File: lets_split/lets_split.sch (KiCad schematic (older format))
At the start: 56 parts, among them P1 USB-rewire, P2 USB_OTG, P3 WS2812-Strip, P4 TRRS jack, SW1 SW_PUSH, SW10 SW_PUSH, SW11 SW_PUSH, SW12 SW_PUSH, SW13 SW_PUSH, SW14 SW_PUSH, SW15 SW_PUSH, SW16 SW_PUSH, SW17 SW_PUSH, SW18 SW_PUSH, SW19 SW_PUSH, SW2 SW_PUSH, SW20 SW_PUSH, SW21 SW_PUSH, SW22 SW_PUSH, SW23 SW_PUSH, SW24 SW_PUSH, SW3 SW_PUSH, SW4 SW_PUSH, SW5 SW_PUSH, SW6 SW_PUSH, SW7 SW_PUSH, SW8 SW_PUSH, SW9 SW_PUSH, U1 ArduinoProMicro

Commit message: Added images of reversible version
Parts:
- P2: symbol USB_OTG -> USB_OTG-RESCUE-lets_split
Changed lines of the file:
@@
-EESchema Schematic File Version 3
+EESchema Schematic File Version 2
+LIBS:lets_split-rescue
 LIBS:power
 LIBS:device
+LIBS:transistors
+LIBS:conn
 LIBS:linear
 LIBS:regul
+LIBS:74xx
+LIBS:cmos4000
 LIBS:adc-dac
 LIBS:memory
@@
 LIBS:digital-audio
 LIBS:philips
+LIBS:display
 LIBS:cypress
 LIBS:siliconi
@@
 LIBS:atmel
 LIBS:contrib
+LIBS:valves
 LIBS:8Bit-MCU
 LIBS:lets_split-cache
@@
 Connection ~ 2275 4550
 $Comp
-L USB_OTG P2
+L USB_OTG-RESCUE-lets_split P2
 U 1 1 59DD5ACB
 P 1825 4125

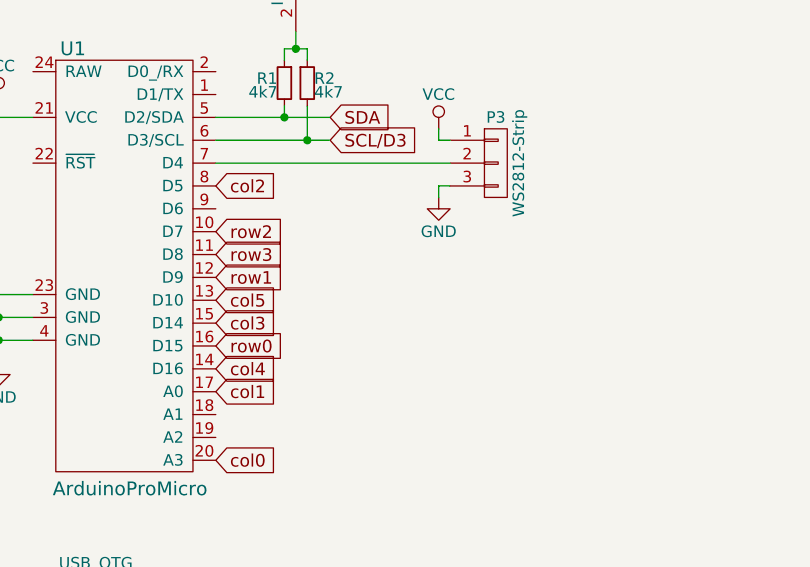
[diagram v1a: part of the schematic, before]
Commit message: Added speaker output to the board
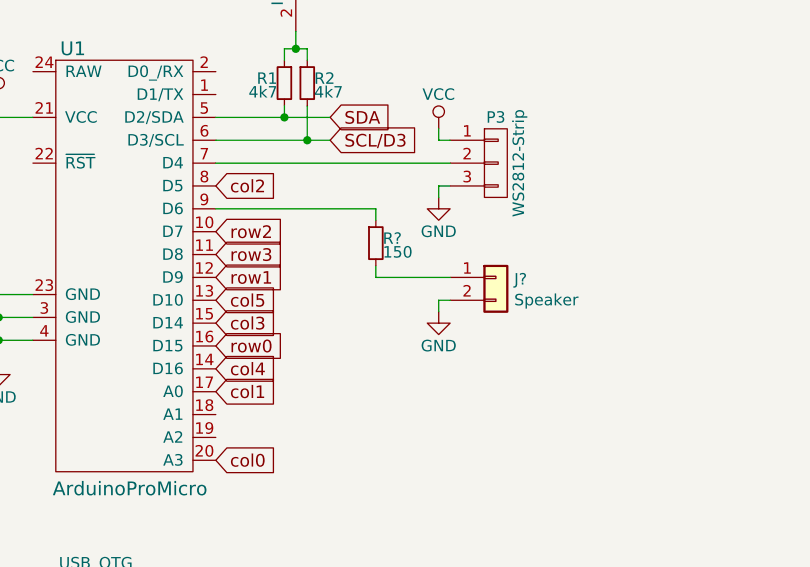
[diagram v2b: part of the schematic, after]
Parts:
- added J?: Speaker, symbol Conn_01x02
- added R?: 150, Resistors_ThroughHole:R_Axial_DIN0207_L6.3mm_D2.5mm_P10.16mm_Horizontal, symbol R_Small
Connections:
- net GND: now also J?.2 (Pin_2)
- net at U1.9 (D6): now also R?.1
- new net: J?.1 (Pin_1), R?.2
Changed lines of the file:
@@
 	1    0    0    1
 $EndComp
+$Comp
+L Conn_01x02 J?
+U 1 1 59E67AC9
+P 3575 2675
+F 0 "J?" H 3655 2667 50  0000 L CNN
+F 1 "Speaker" H 3655 2576 50  0000 L CNN
+F 2 "" H 3575 2675 50  0001 C CNN
+F 3 "" H 3575 2675 50  0001 C CNN
+	1    3575 2675
+	1    0    0    -1
+$EndComp
+$Comp
+L GND #PWR?
+U 1 1 59E67C6F
+P 3325 2825
+F 0 "#PWR?" H 3325 2575 50  0001 C CNN
+F 1 "GND" H 3325 2675 50  0000 C CNN
+F 2 "" H 3325 2825 50  0000 C CNN
+F 3 "" H 3325 2825 50  0000 C CNN
+	1    3325 2825
+	1    0    0    -1
+$EndComp
+Wire Wire Line
+	3375 2775 3325 2775
+Wire Wire Line
+	3325 2775 3325 2825
+Wire Wire Line
+	2350 2375 3050 2375
+Wire Wire Line
+	3050 2675 3375 2675
+$Comp
+L R_Small R?
+U 1 1 59E680B3
+P 3050 2525
+F 0 "R?" H 3080 2545 50  0000 L CNN
+F 1 "150" H 3080 2485 50  0000 L CNN
+F 2 "Resistors_ThroughHole:R_Axial_DIN0207_L6.3mm_D2.5mm_P10.16mm_Horizontal" H 3050 2525 50  0001 C CNN
+F 3 "" H 3050 2525 50  0000 C CNN
+	1    3050 2525
+	1    0    0    -1
+$EndComp
+Wire Wire Line
+	3050 2625 3050 2675
+Wire Wire Line
+	3050 2375 3050 2425
 $EndSCHEMATC

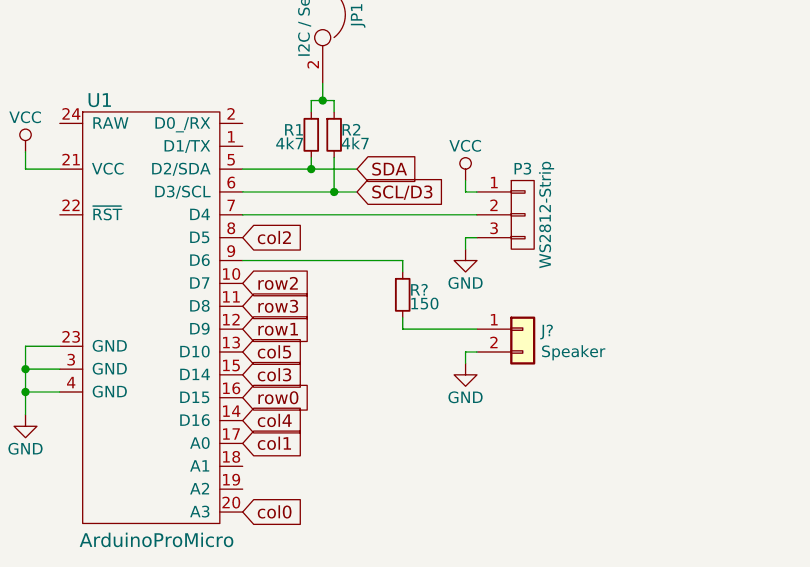
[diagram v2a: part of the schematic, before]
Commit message: Connected speaker to correct pin
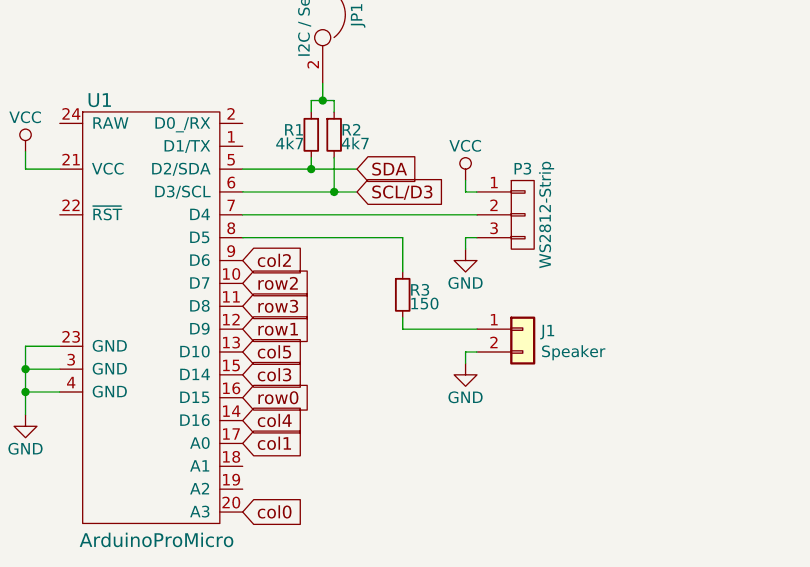
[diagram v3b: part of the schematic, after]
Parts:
- J1: renamed from J?; footprint (none) -> Buzzers_Beepers:Buzzer_12x9.5RM7.6
- R3: renamed from R?; footprint Resistors_ThroughHole:R_Axial_DIN0207_L6.3mm_D2.5mm_P10.16mm_Horizontal -> Resistors_SMD:R_0603_HandSoldering
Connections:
- net col2: now also U1.9 (D6); no longer U1.8 (D5)
- net at R3.1: now also U1.8 (D5); no longer U1.9 (D6)
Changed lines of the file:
@@
 Text GLabel 2350 3175 2    55   Input ~ 0
 col1
-Text GLabel 2350 2275 2    55   Input ~ 0
+Text GLabel 2350 2375 2    55   Input ~ 0
 col2
 Text GLabel 2350 2875 2    55   Input ~ 0
@@
 $EndComp
 $Comp
-L Conn_01x02 J?
+L Conn_01x02 J1
 U 1 1 59E67AC9
 P 3575 2675
-F 0 "J?" H 3655 2667 50  0000 L CNN
+F 0 "J1" H 3655 2667 50  0000 L CNN
 F 1 "Speaker" H 3655 2576 50  0000 L CNN
-F 2 "" H 3575 2675 50  0001 C CNN
+F 2 "Buzzers_Beepers:Buzzer_12x9.5RM7.6" H 3575 2675 50  0001 C CNN
 F 3 "" H 3575 2675 50  0001 C CNN
 	1    3575 2675
@@
 $EndComp
 $Comp
-L GND #PWR?
+L GND #PWR09
 U 1 1 59E67C6F
 P 3325 2825
-F 0 "#PWR?" H 3325 2575 50  0001 C CNN
+F 0 "#PWR09" H 3325 2575 50  0001 C CNN
 F 1 "GND" H 3325 2675 50  0000 C CNN
 F 2 "" H 3325 2825 50  0000 C CNN
@@
 	3325 2775 3325 2825
 Wire Wire Line
-	2350 2375 3050 2375
-Wire Wire Line
 	3050 2675 3375 2675
 $Comp
-L R_Small R?
+L R_Small R3
 U 1 1 59E680B3
 P 3050 2525
-F 0 "R?" H 3080 2545 50  0000 L CNN
+F 0 "R3" H 3080 2545 50  0000 L CNN
 F 1 "150" H 3080 2485 50  0000 L CNN
-F 2 "Resistors_ThroughHole:R_Axial_DIN0207_L6.3mm_D2.5mm_P10.16mm_Horizontal" H 3050 2525 50  0001 C CNN
+F 2 "Resistors_SMD:R_0603_HandSoldering" H 3050 2525 50  0001 C CNN
 F 3 "" H 3050 2525 50  0000 C CNN
 	1    3050 2525
@@
 	3050 2625 3050 2675
 Wire Wire Line
-	3050 2375 3050 2425
+	3050 2275 3050 2425
+Wire Wire Line
+	2350 2275 3050 2275
 $EndSCHEMATC

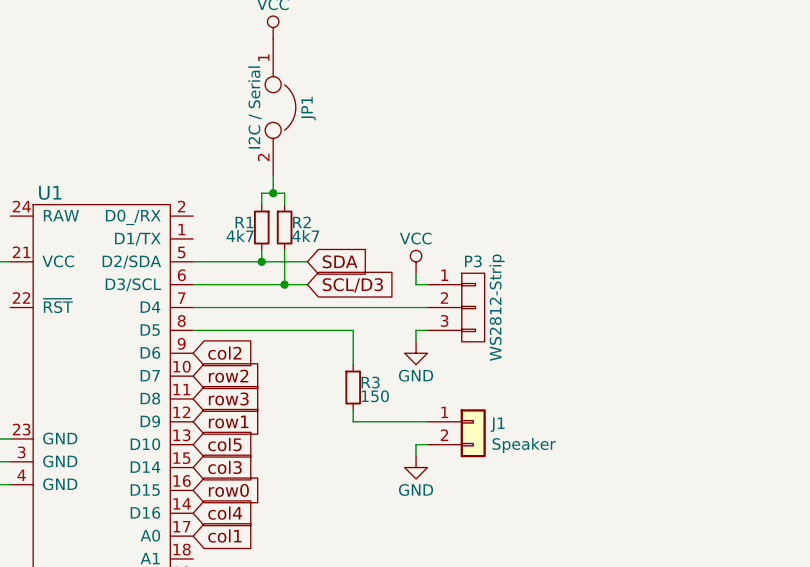
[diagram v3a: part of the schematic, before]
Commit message: Fixed some stupid mistakes (traces over holes)
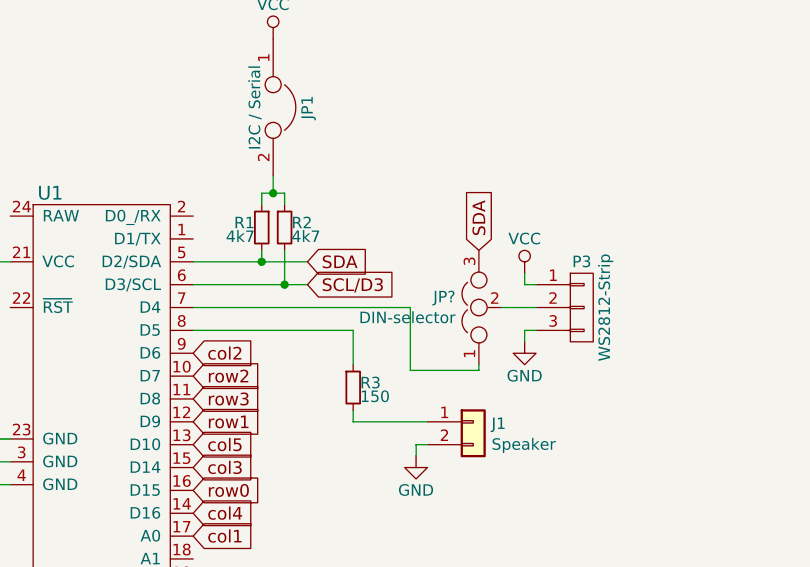
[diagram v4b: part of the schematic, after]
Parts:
- added JP?: DIN-selector, symbol Jumper_NC_Dual
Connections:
- net SDA: now also JP?.3
- net at U1.7 (D4): now also JP?.1; no longer P3.2 (P2)
- new net: JP?.2, P3.2 (P2)
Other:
- moved on the sheet: P3
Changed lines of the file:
@@
 L CONN_01X03 P3
 U 1 1 59DDE6F8
-P 3575 2175
-F 0 "P3" H 3575 2375 50  0000 C CNN
-F 1 "WS2812-Strip" V 3675 2175 50  0000 C CNN
-F 2 "Wirepads:SMD_PAD_1x03_Pitch2.54mm" H 3575 2175 50  0001 C CNN
-F 3 "" H 3575 2175 50  0000 C CNN
-	1    3575 2175
+P 4050 2175
+F 0 "P3" H 4050 2375 50  0000 C CNN
+F 1 "WS2812-Strip" V 4150 2175 50  0000 C CNN
+F 2 "Wirepads:SMD_PAD_1x03_Pitch2.54mm" H 4050 2175 50  0001 C CNN
+F 3 "" H 4050 2175 50  0000 C CNN
+	1    4050 2175
 	1    0    0    -1
 $EndComp
@@
 L VCC #PWR07
 U 1 1 59DDEE69
-P 3325 2025
-F 0 "#PWR07" H 3325 1875 50  0001 C CNN
-F 1 "VCC" H 3325 2175 50  0000 C CNN
-F 2 "" H 3325 2025 50  0000 C CNN
-F 3 "" H 3325 2025 50  0000 C CNN
-	1    3325 2025
+P 3800 2025
+F 0 "#PWR07" H 3800 1875 50  0001 C CNN
+F 1 "VCC" H 3800 2175 50  0000 C CNN
+F 2 "" H 3800 2025 50  0000 C CNN
+F 3 "" H 3800 2025 50  0000 C CNN
+	1    3800 2025
 	1    0    0    -1
 $EndComp
@@
 L GND #PWR08
 U 1 1 59DDF0E6
-P 3325 2325
-F 0 "#PWR08" H 3325 2075 50  0001 C CNN
-F 1 "GND" H 3325 2175 50  0000 C CNN
-F 2 "" H 3325 2325 50  0000 C CNN
-F 3 "" H 3325 2325 50  0000 C CNN
-	1    3325 2325
+P 3800 2325
+F 0 "#PWR08" H 3800 2075 50  0001 C CNN
+F 1 "GND" H 3800 2175 50  0000 C CNN
+F 2 "" H 3800 2325 50  0000 C CNN
+F 3 "" H 3800 2325 50  0000 C CNN
+	1    3800 2325
 	1    0    0    -1
 $EndComp
 Wire Wire Line
-	3325 2025 3325 2075
+	3800 2025 3800 2075
 Wire Wire Line
-	3325 2075 3375 2075
+	3800 2075 3850 2075
 Wire Wire Line
-	3325 2325 3325 2275
+	3800 2325 3800 2275
 Wire Wire Line
-	3325 2275 3375 2275
-Wire Wire Line
-	2350 2175 3375 2175
+	3800 2275 3850 2275
 $Comp
 L CONN_01X06 P4
@@
 Wire Wire Line
 	2350 2275 3050 2275
+$Comp
+L Jumper_NC_Dual JP?
+U 1 1 59E6A06B
+P 3600 2175
+F 0 "JP?" V 3646 2277 50  0000 L CNN
+F 1 "DIN-selector" V 3555 2277 50  0000 L CNN
+F 2 "" H 3600 2175 50  0001 C CNN
+F 3 "" H 3600 2175 50  0001 C CNN
+	1    3600 2175
+	0    -1   -1   0
+$EndComp
+Wire Wire Line
+	2350 2175 3300 2175
+Wire Wire Line
+	3300 2175 3300 2450
+Wire Wire Line
+	3300 2450 3600 2450
+Wire Wire Line
+	3600 2450 3600 2425
+Wire Wire Line
+	3700 2175 3850 2175
+Text GLabel 3600 1925 1    55   Input ~ 0
+SDA
 $EndSCHEMATC
